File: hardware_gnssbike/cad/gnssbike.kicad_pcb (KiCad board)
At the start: 4 copper layers, 55 x 97 mm, 117 parts, among them J101 Molex 2036150003, J102 JST SM06B-GHS-TB, J103 contato de mola, 2 vias, J104 contato de mola, 2 vias, J105 contato de mola, 2 vias, J201 Tag-Connect TC2030-NL, J302 contato de mola, 2 vias, J401 Hirose FH28-10S-0.5SH, J402 Molex 503480-0500, Q401 DMG1012T-7, Q601 DMG1012T-7, Q602 DMG1012T-7, Q603 DMG1012T-7, SW601 Omron B3S-1002P, SW602 Omron B3S-1002P, SW603 Omron B3S-1002P, U101 nPM1300-QEAA, U102 MAX17262REWL, U103 AEM10900, U104 TPS7A0218PDQN, U201 MinewSemi ME54BS13, U301 u-blox MAX-F10S, U302 TI TXU0204BQAR, U501 MX25R6435F, U502 Bosch BMP585, U503 Bosch BMI270, U504 MMC5633NJL, U505 TI OPT3001DNPR

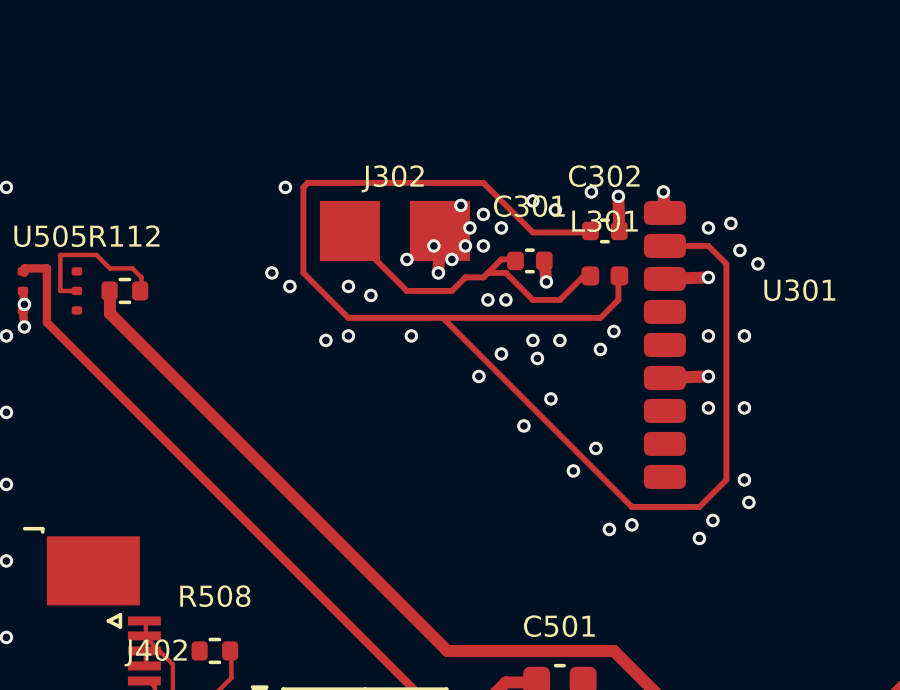
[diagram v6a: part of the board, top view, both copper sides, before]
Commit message: fix(hardware): each package built from its own datasheet's drawing
The bodies were built from the footprint outline and a height table, and a
land pattern is not a package: it is deliberately bigger than the part that
sits on it. Where the height came from the part's own datasheet it said so,
but six of them said "usual for the package" instead, which is a guess
wearing a number.

Six packages now carry the dimensions their own mechanical drawing gives,
each with the document and the drawing cited beside it:

  AEM10900 QFN-28   4.00 x 4.00 x 0.80, exposed pad 2.60 x 2.60, terminal
                    0.20 x 0.40, pitch 0.40   (DS-AEM1090x-v2.4.0, fig. 29)
  TPS7A02 X2SON-4   1.00 x 1.00 x 0.48, standoff 0.03, pitch 0.65
                    (SBVS277C, DQN0004A)
  TXU0204 WQFN-14   3.00 x 2.50 x 0.75, exposed pad 1.50 x 1.00, pitch 0.50
                    (SCES936A, BQA0014A)
  OPT3001 USON-6    2.00 x 2.00 x 0.60, exposed pad 0.65 x 1.35, pitch 0.65
                    (SBOS681B, DNP0006A)
  TPD4E05U06        2.50 x 1.00 x 0.40, pitch 0.50   (DQA0010A)
  SOT-523           D 1.60, E1 0.80, A2 0.75, A1 0.05, b 0.22, e 0.50 BSC
                    (Diodes DS31783 Rev. 8)

Three of those heights were wrong before: the harvester's QFN was drawn
0.90 mm against its real 0.80, the ESD array 0.55 against 0.40, and the
regulator 0.40 against 0.48. The exposed pads were worse - they were half the
body, whatever the body was, where the AEM10900's is 2.60 of 4.00 and the
OPT3001's is a 0.65 x 1.35 rectangle and not a square at all.

And the two drawings now have to agree. ME3 compares, for every package with
a datasheet dimension, the body against the outline the footprint was drawn
with: too big and it does not fit its own land pattern, too small and the
footprint was meant for another part. Orientation is ignored, because a
footprint may stand a package on end, which the TPD4E05U06 does. Thirteen of
the fourteen measured rules pass and the DRC reports no error.
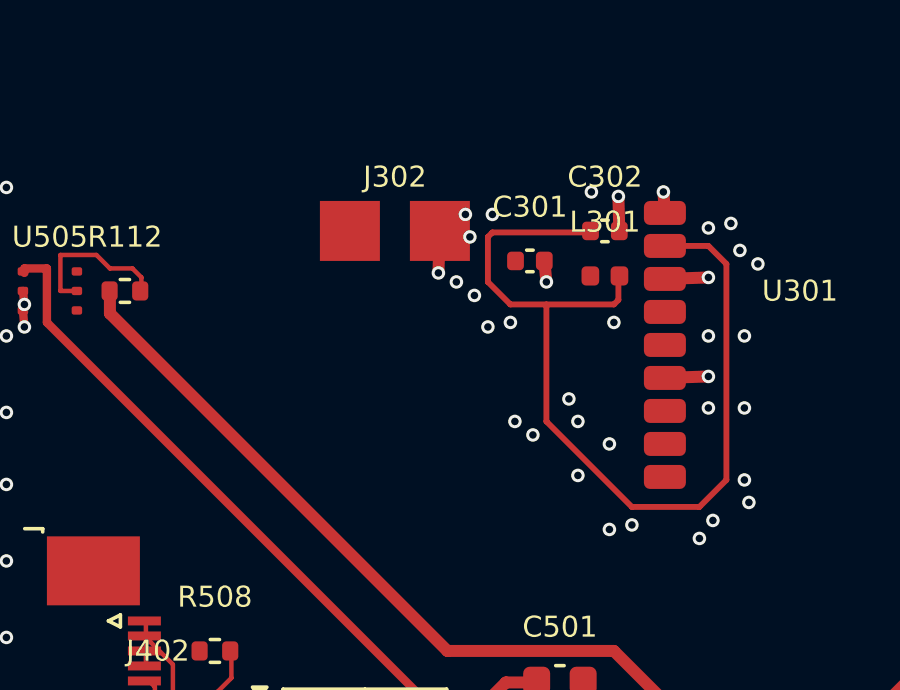
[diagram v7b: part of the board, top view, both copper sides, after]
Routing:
- net RF_IN: track 47.3 -> 31.5 mm
- net RF_ANT: track 10.9 -> 0.00 mm
- net GND: vias 197 -> 179

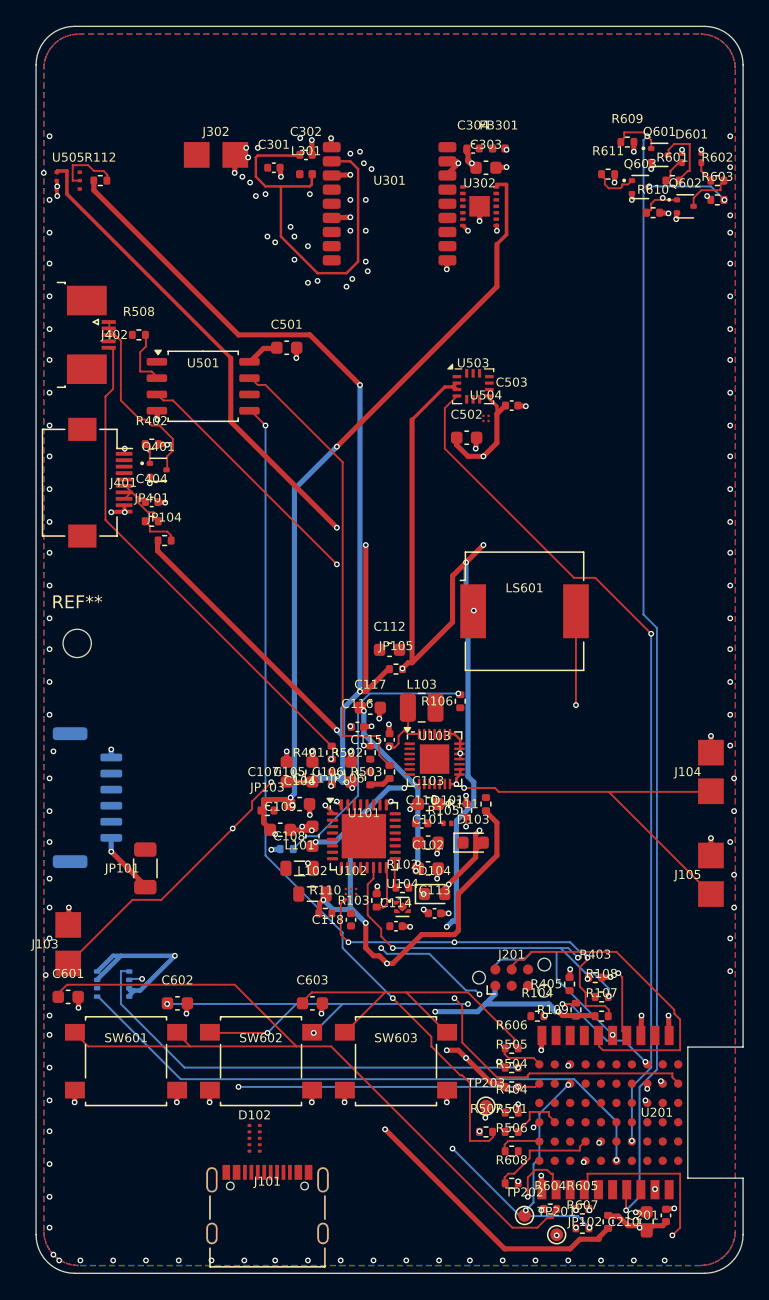
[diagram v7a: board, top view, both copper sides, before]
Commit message: fix(hardware): draw every package from its own datasheet, and fill the pours
The 3D view drew twenty-three parts as the same black cuboid of the
courtyard's size. kicad-cli's GLB export reads STEP only, so the VRML
bodies this project writes never reached it, and make_3d.py built its own
boxes in one hard coded colour - which made the radio module, the GNSS
receiver, the three keys, the buzzer and the USB-C receptacle five
identical bricks in the view that exists to check that a part is the part
you think it is. It now reads the .wrl: shape and colour both. 264
triangles became 3588.

With that fixed the bodies themselves are worth drawing. Three more
packages carry the cotes of their own mechanical drawing - the
MX25R6435F in SOP 8L 200MIL, the BMI270 in LGA-14 and the APTF1616, which
stops being a block and becomes a white housing with a water-clear lens -
for eleven in all, each with the figure it came from, and ME3 checks the
body against the outline drawn for it. The four spring contacts had no
body at all; they get a gold leaf over each pad, with the height declared
as NOT read from any datasheet, because no spring has been chosen. The
FPC connector gets its ivory housing and dark latch.

Two rules were being measured on a board that was not there. The
generators write a ground zone as an outline and nothing else, which is
legal - KiCad fills on open - but kicad-cli pcb drc does not fill, so
every pad that reaches only the plane read as unconnected and every
stitching via as dangling, and no clearance was ever measured against the
pour. fill_zones.py calls KiCad's own filler through pcbnew. Unconnected
went from 296 to 100 and eleven real starved thermals appeared, which the
ground pads now avoid by connecting solid: this board is reflow
assembled, nothing on it can be hand soldered, and a single 0.3 mm spoke
is a needless neck in the return current of the USB shell and the MCU.

And the 20 mm between the module and a switching converter, which this
session de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
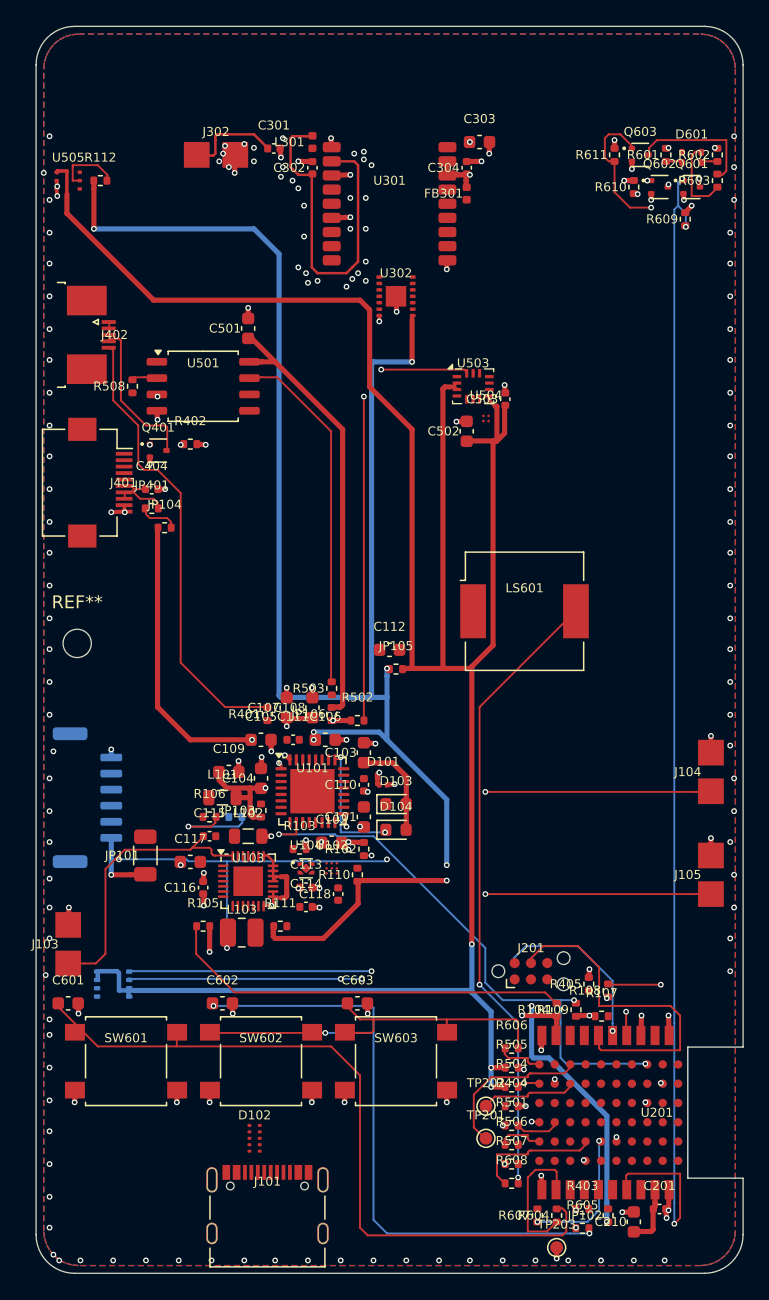
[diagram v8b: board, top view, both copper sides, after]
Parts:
- moved L103 22.4 mm to (41.0, 95.5)
- moved R105 22.4 mm to (38.0, 95.0), turned to 0 degrees
- moved R106 21.5 mm to (38.5, 86.5), turned to 0 degrees
- moved R111 18.6 mm to (44.0, 95.0), turned to 0 degrees
- moved C117 18.4 mm to (37.0, 90.0)
- moved R403 18.0 mm to (67.5, 117.0)
- moved U103 17.3 mm to (41.5, 91.5)
- moved C116 17.3 mm to (38.0, 92.0), turned to 90 degrees
- moved C115 15.9 mm to (38.5, 88.0), turned to 0 degrees
- moved TP203 12.3 mm to (65.5, 120.0)
- moved C113 10.2 mm to (46.0, 92.0)
- moved C108 10.0 mm to (46.5, 78.0)
- moved U302 9.55 mm to (53.0, 46.0)
- moved TP201 9.30 mm to (60.0, 111.5)
- moved TP202 9.01 mm to (60.0, 109.0)
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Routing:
- net RGB_G: track 97.7 -> 1.96 mm
- net RGB_B: track 3.43 -> 84.9 mm, vias 0 -> 2
- net DISP_SCK: track 77.8 -> 0.00 mm, vias 4 -> 0
- net VSYS: track 75.3 -> 7.93 mm, vias 4 -> 0
- net IMU_INT: track 66.5 -> 0.00 mm, vias 2 -> 0
- net NOR_MOSI_F: track 66.4 -> 0.00 mm, vias 2 -> 0
- net 1V8: track 69.2 -> 11.5 mm, vias 6 -> 2
- net SENS_SDA: track 36.1 -> 93.3 mm, vias 3 -> 4
- net PWR_SDA: track 56.3 -> 0.00 mm, vias 4 -> 0
- net BUZ_A_LS: track 56.0 -> 0.00 mm, vias 3 -> 0
- net BARO_INT: track 47.4 -> 0.00 mm, vias 1 -> 0
- net SD3V0: track 1.69 -> 45.5 mm, vias 0 -> 2
- net PMIC_INT: track 9.58 -> 43.9 mm, vias 2 -> 3
- net SD3V0_FLASH: track 2.53 -> 34.6 mm
- net VBUSOUT: track 0.00 -> 31.7 mm, vias 0 -> 2
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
